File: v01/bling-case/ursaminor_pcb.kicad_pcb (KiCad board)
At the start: 2 copper layers, 298.6 x 118.1 mm, 209 parts, among them J1 USB_C_Receptacle_USB2.0, J2 I2C-L, J3 I2C-R, J4 AVR-ISP-6, SW1 Reset, U1 ATmega32U4-AU, U2 MCP23017_SO, U3 IS31FL3733-TQ, U4 IS31FL3733-TQ, U5 PRTR5V0U2X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

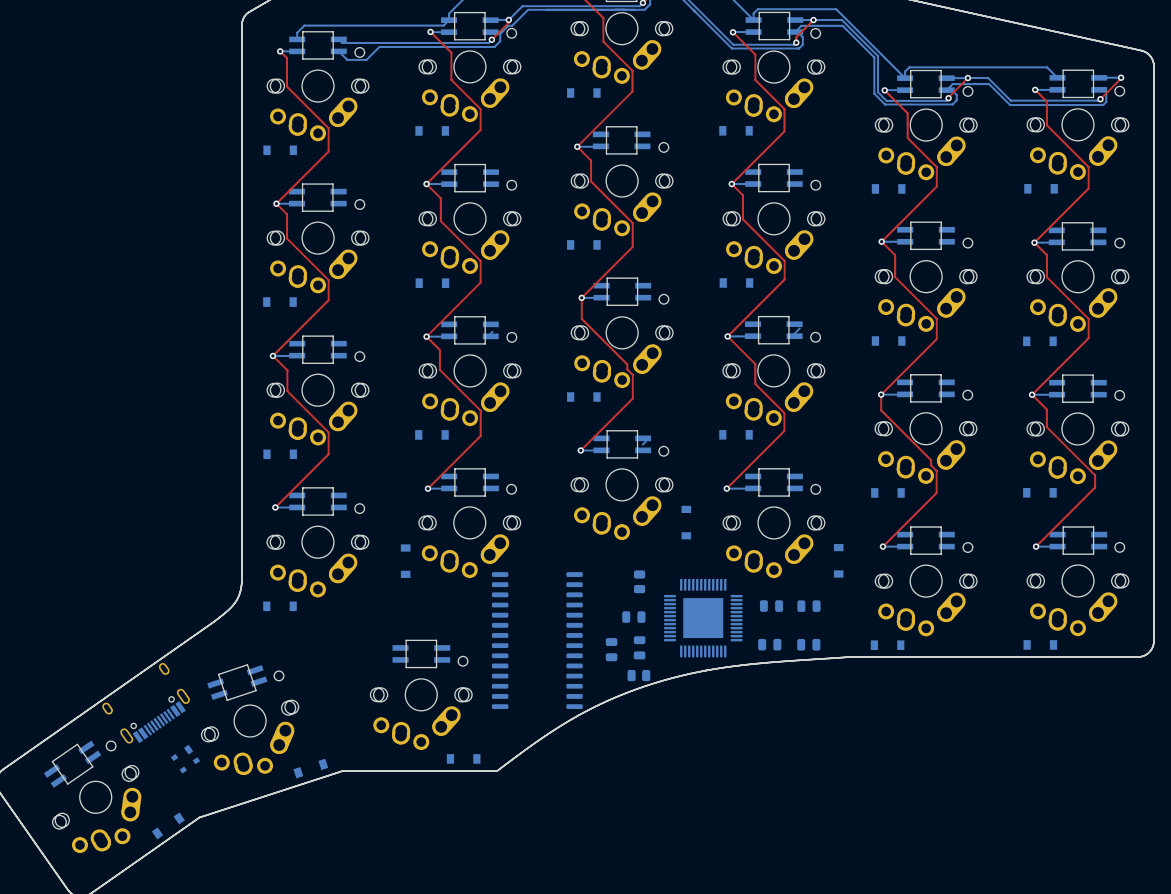
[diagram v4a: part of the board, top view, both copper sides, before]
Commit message: Complete more routing on the right side.
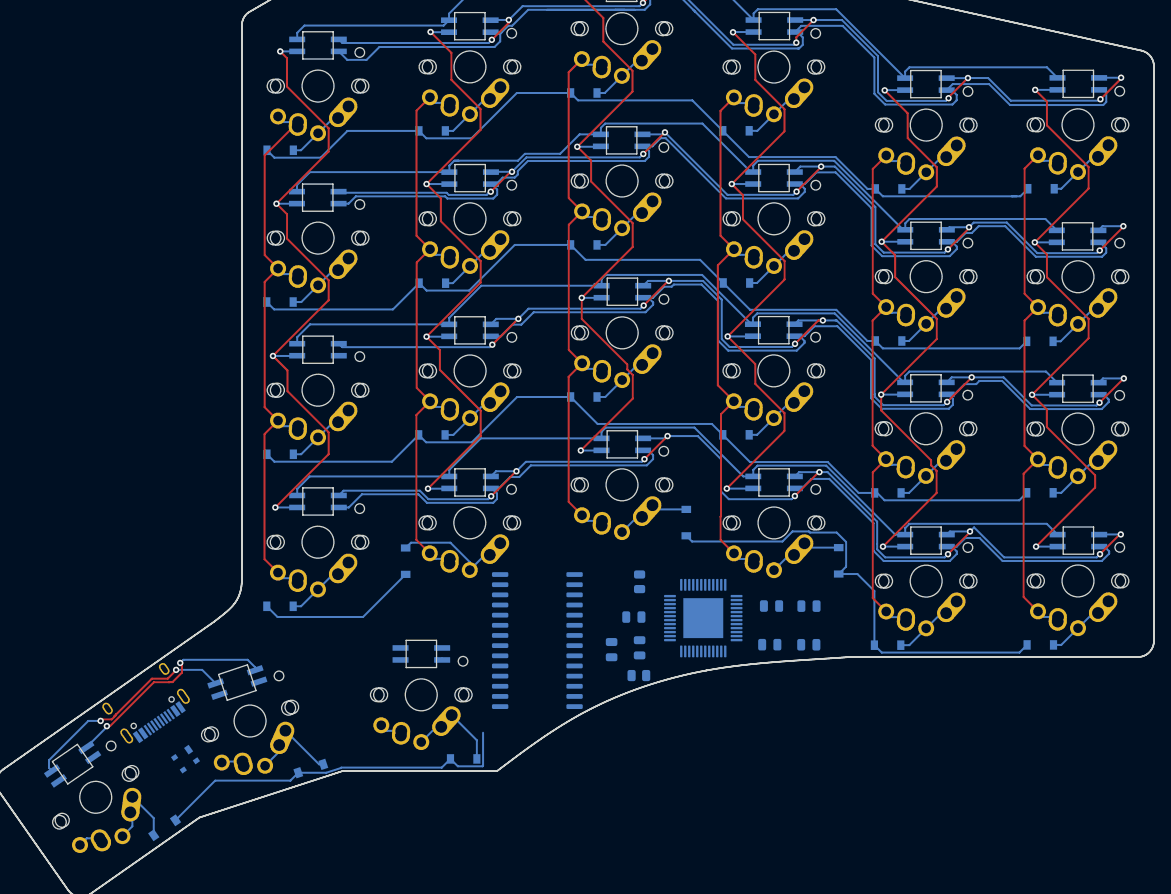
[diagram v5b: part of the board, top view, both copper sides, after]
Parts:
- moved D52 0.53 mm to (188.9, 125.1), turned to 214.5 degrees
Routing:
- net Right-SW2: track 0.90 -> 163.2 mm, vias 0 -> 12
- net Right-SW5: track 0.00 -> 138.6 mm, vias 0 -> 10
- net Right-SW3: track 0.00 -> 136.9 mm, vias 0 -> 2
- net Right-SW8: track 0.00 -> 133.5 mm, vias 0 -> 10
- net Right-SW7: track 0.00 -> 125.9 mm
- net Right-SW9: track 0.00 -> 109.1 mm
- net Right-SW6: track 0.00 -> 108.8 mm
- net Row0-R: track 0.00 -> 105.9 mm
- net Right-SW4: track 1.52 -> 106.9 mm
- net Row2-R: track 0.00 -> 105.2 mm
- net Row1-R: track 0.00 -> 105.2 mm
- net Right-SW1: track 0.22 -> 100.1 mm
- net Row3-R: track 0.00 -> 77.8 mm
- net Col8: track 0.40 -> 76.0 mm
- net Col6: track 0.00 -> 75.5 mm
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
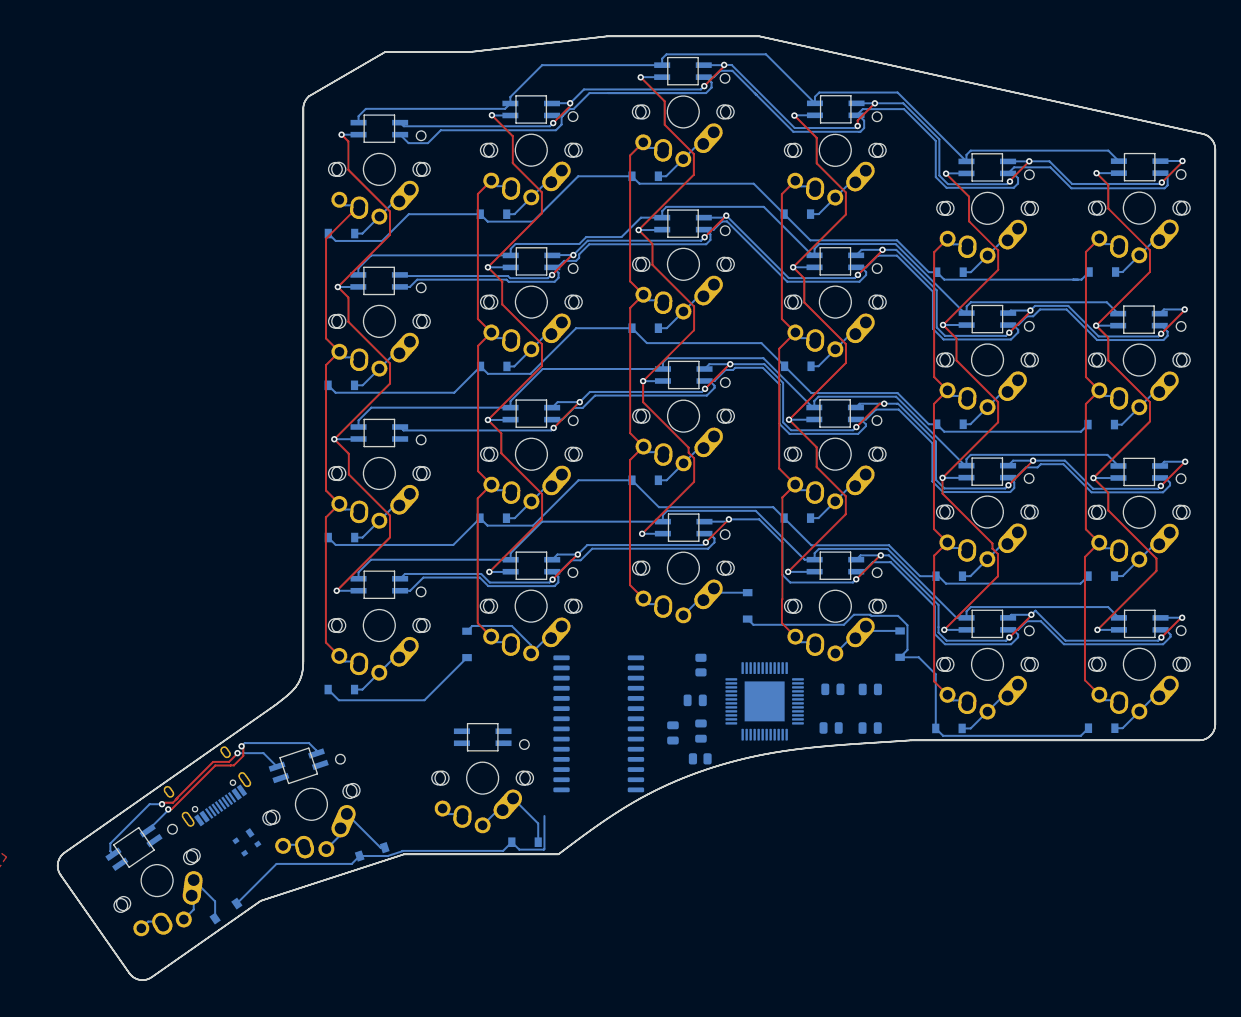
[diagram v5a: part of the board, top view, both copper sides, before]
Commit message: Route the data lines and some of the RGB matrix on the right side.
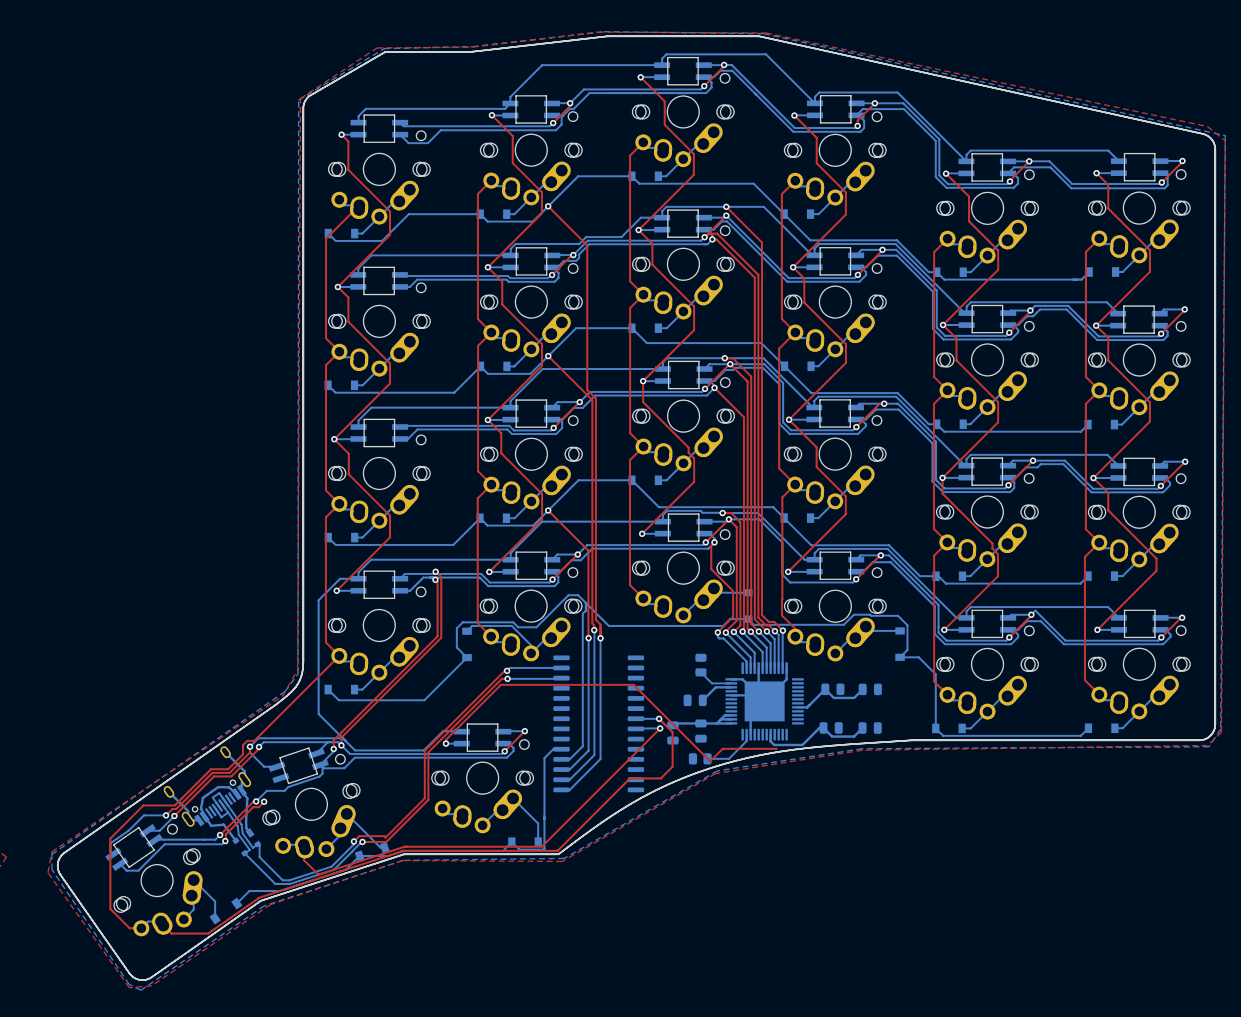
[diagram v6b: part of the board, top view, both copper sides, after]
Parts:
- moved D108 0.05 mm to (220.9, 108.5)
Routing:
- net Col6: track 75.5 -> 208.3 mm, vias 0 -> 1
- net Right-SW1: track 100.1 -> 202.3 mm, vias 0 -> 6
- net Right-SW2: track 163.2 -> 243.6 mm, vias 12 -> 17
- net Row0-R: track 105.9 -> 185.6 mm, vias 0 -> 2
- net Right-SW3: track 136.9 -> 213.8 mm, vias 2 -> 4
- net Row3-R: track 77.8 -> 145.0 mm
- net SDA-R: track 0.00 -> 66.3 mm, vias 0 -> 2
- net SCL-R: track 0.00 -> 64.7 mm, vias 0 -> 2
- net Right-SW9: track 109.1 -> 170.1 mm, vias 0 -> 2
- net Right-SW4: track 106.9 -> 166.9 mm, vias 0 -> 2
- net Right-SW8: track 133.5 -> 193.0 mm, vias 10 -> 11
- net Right-SW7: track 125.9 -> 183.9 mm, vias 0 -> 2
- net Row1-R: track 105.2 -> 162.9 mm, vias 0 -> 2
- net Col7: track 75.7 -> 133.0 mm, vias 0 -> 1
- net VBUS: track 0.00 -> 53.0 mm
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- added copper zone on B.Cu, net VSS
- added copper zone on F.Cu, net VSS

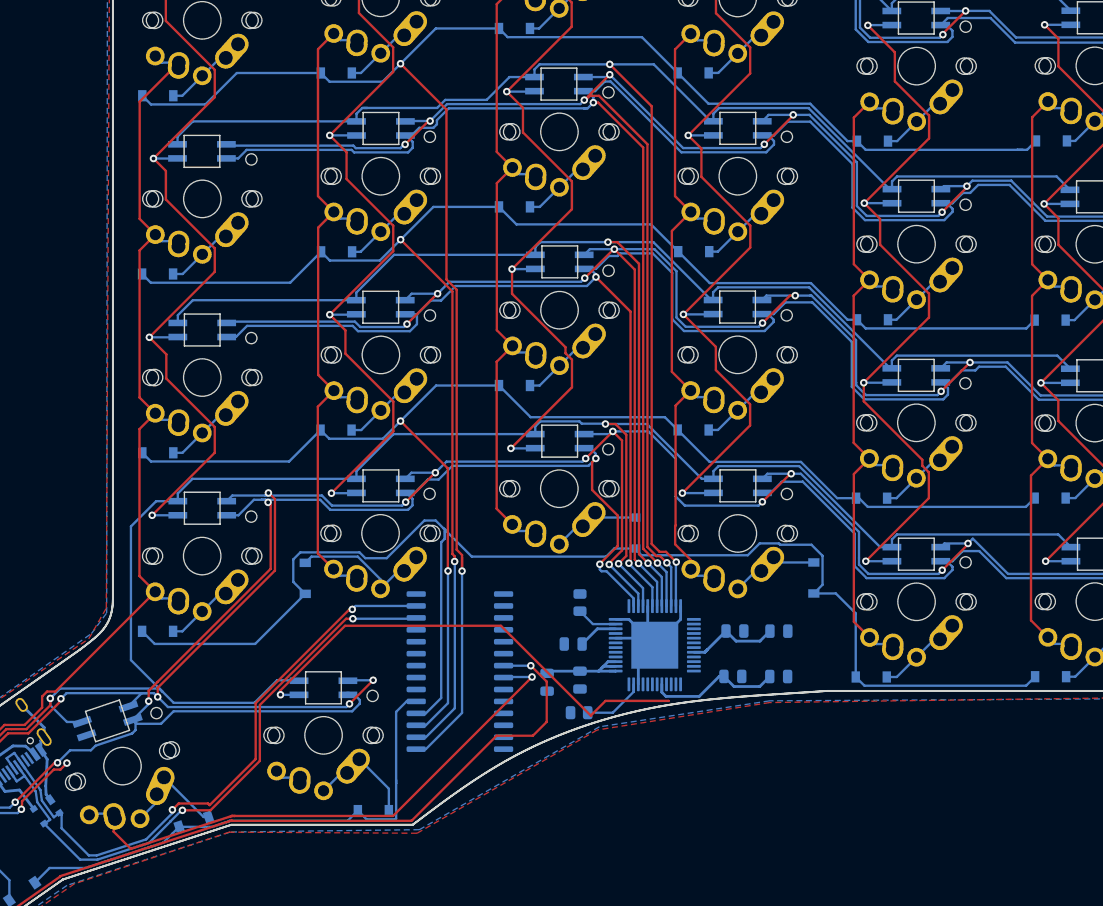
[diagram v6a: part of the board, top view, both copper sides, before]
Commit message: More routing on the right side.
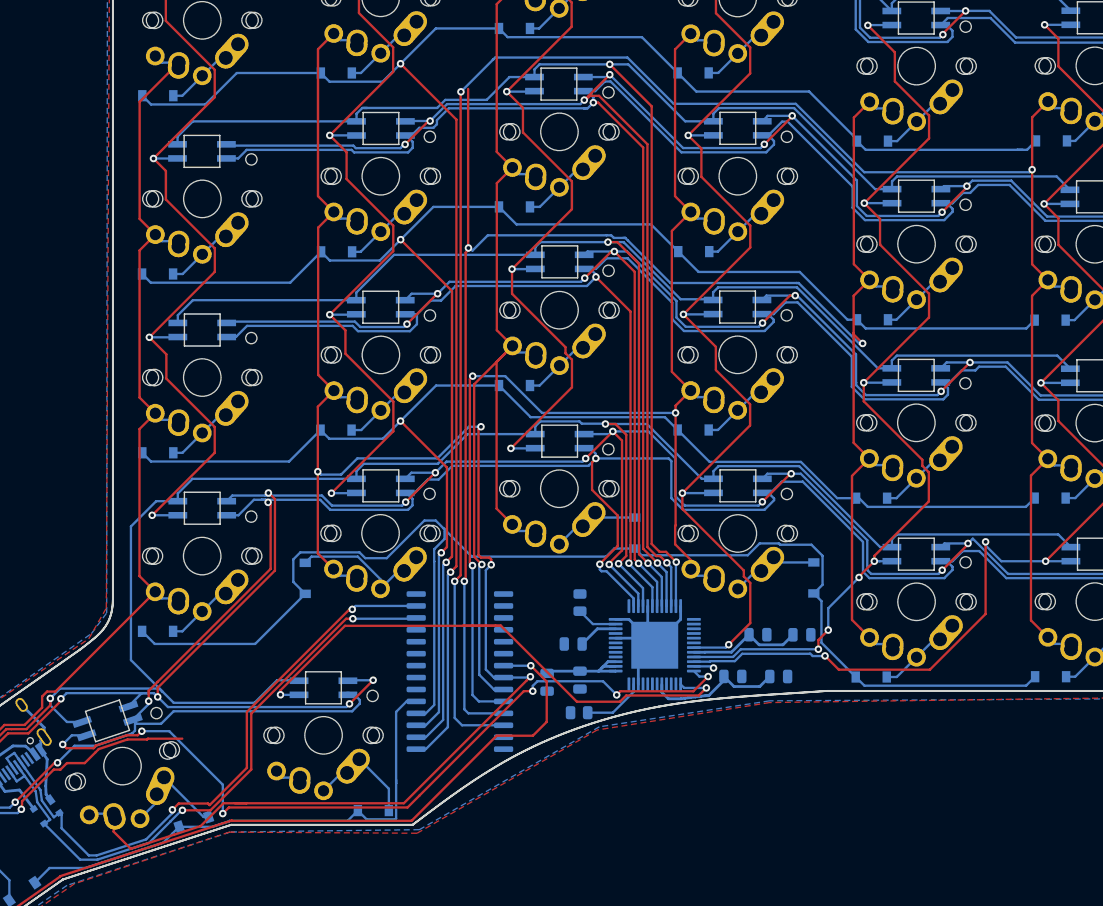
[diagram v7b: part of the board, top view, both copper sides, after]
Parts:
- moved C9 2.48 mm to (271.9, 97.8)
- moved C15 2.48 mm to (267.2, 97.8)
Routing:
- net Col11: track 72.5 -> 212.6 mm, vias 0 -> 3
- net Col10: track 72.6 -> 192.7 mm, vias 0 -> 3
- net Right-CS8: track 0.00 -> 87.1 mm, vias 0 -> 6
- net Col9: track 72.6 -> 133.6 mm, vias 0 -> 3
- net Col7: track 133.0 -> 182.9 mm, vias 1 -> 4
- net Right-CS6: track 86.0 -> 135.7 mm, vias 4 -> 6
- net Col8: track 76.0 -> 115.2 mm, vias 0 -> 1
- net Right-SW1: track 202.3 -> 227.7 mm
- net Right-CS5: track 85.3 -> 109.4 mm, vias 4 -> 7
- net Right-CS4: track 85.8 -> 109.7 mm, vias 4 -> 5
- net Right-CS7: track 22.3 -> 37.6 mm
- net Right-CS9: track 51.2 -> 61.5 mm, vias 1 -> 2
- net Right-SW5: track 178.6 -> 175.3 mm
- net Right-SW4: track 166.9 -> 163.7 mm
- net VBUS: track 53.0 -> 55.1 mm
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
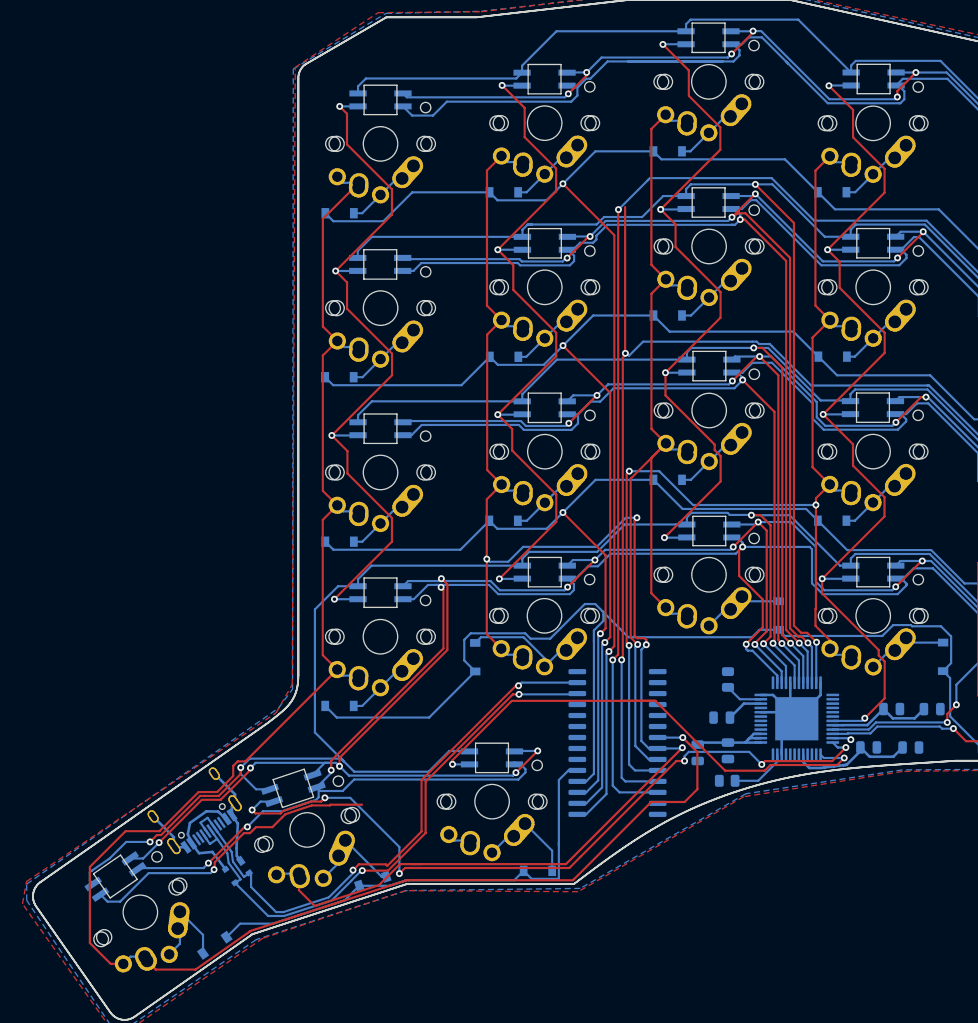
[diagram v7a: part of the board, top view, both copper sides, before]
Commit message: Route more of the right side.
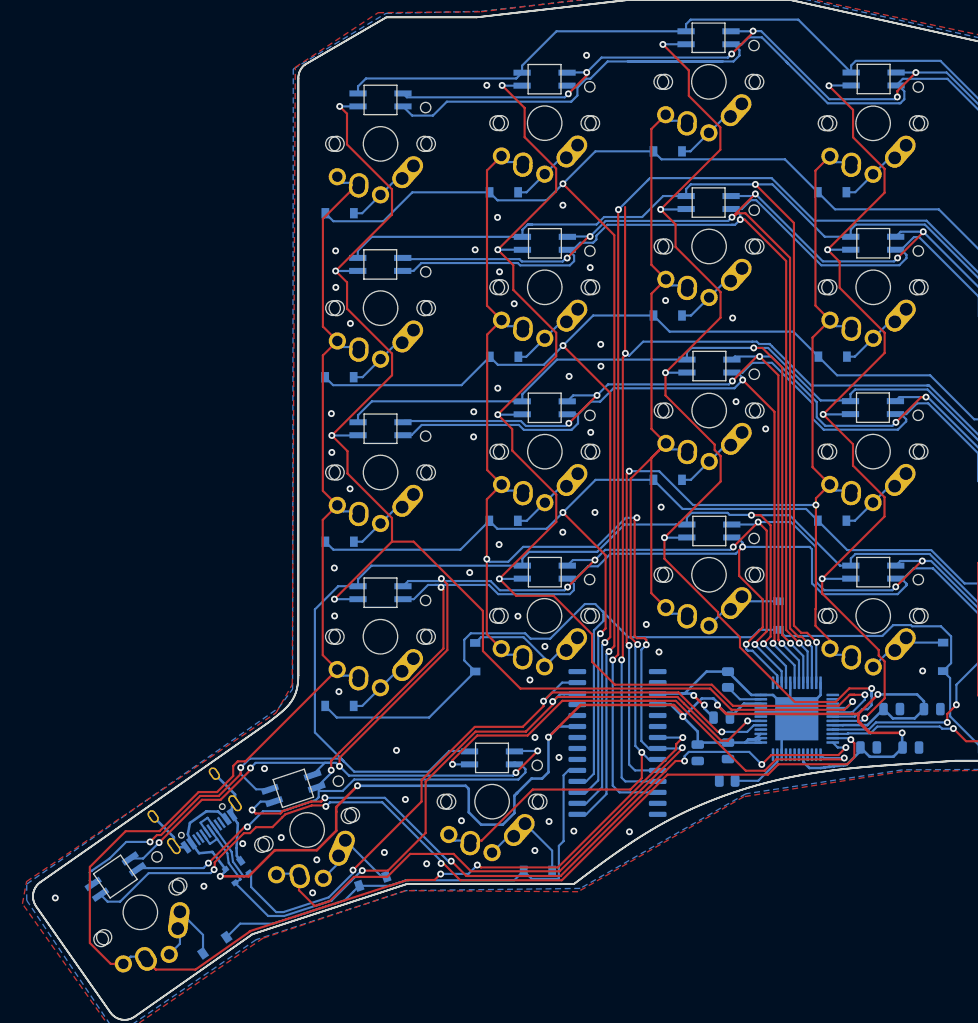
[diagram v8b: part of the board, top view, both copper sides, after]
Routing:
- net VBUS: track 55.1 -> 184.6 mm, vias 0 -> 7
- net Right-CS7: track 37.6 -> 106.7 mm, vias 2 -> 4
- net Right-CS1: track 83.9 -> 151.0 mm, vias 4 -> 5
- net Right-CS2: track 84.3 -> 140.5 mm, vias 4 -> 5
- net Right-CS3: track 84.3 -> 126.6 mm, vias 4 -> 5
- net SCL-R: track 64.7 -> 92.3 mm, vias 2 -> 3
- net SDA-R: track 66.3 -> 92.3 mm, vias 2 -> 3
- net Col8: track 115.2 -> 141.0 mm, vias 1 -> 2
- net VSS: track 40.9 -> 59.9 mm, vias 0 -> 59
- net Col6: track 208.3 -> 203.0 mm, vias 1 -> 3
- net Right-CS8: track 87.1 -> 85.5 mm
- net Col7: track 182.9 -> 183.9 mm
